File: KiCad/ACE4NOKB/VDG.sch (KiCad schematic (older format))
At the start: 32 parts, among them Q1 2N3904, Q100 2N3904, X1 CRYSTALHC49U-V 6.5MHz

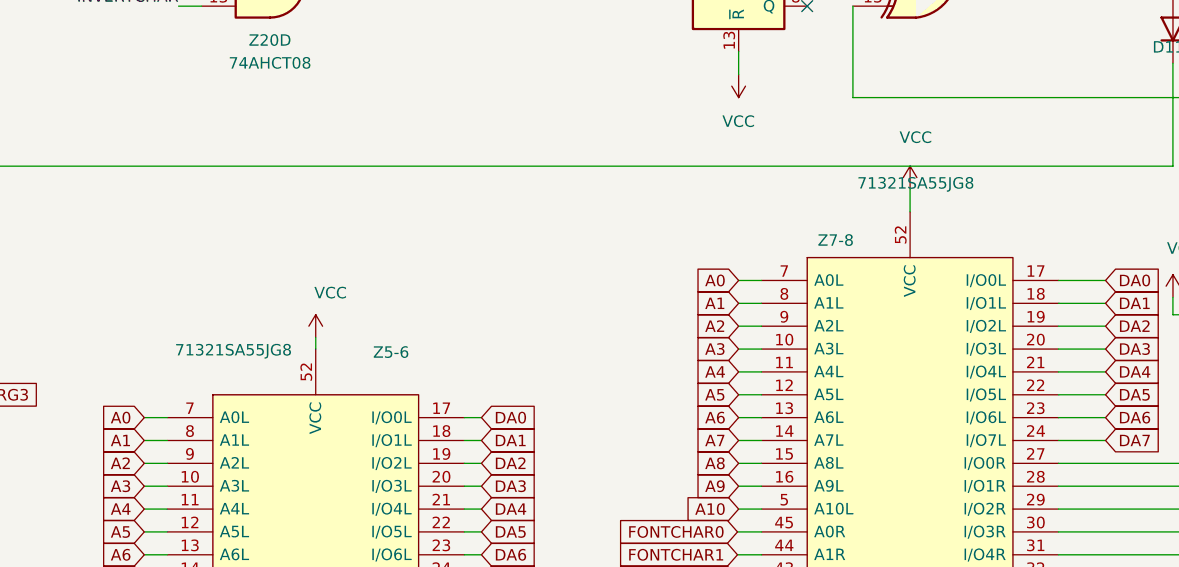
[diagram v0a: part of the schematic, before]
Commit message: Remove SMD.
Standardise Z180 and add Z380.


Signed-off-by: John Bradley <flypie@rocketmail.com>
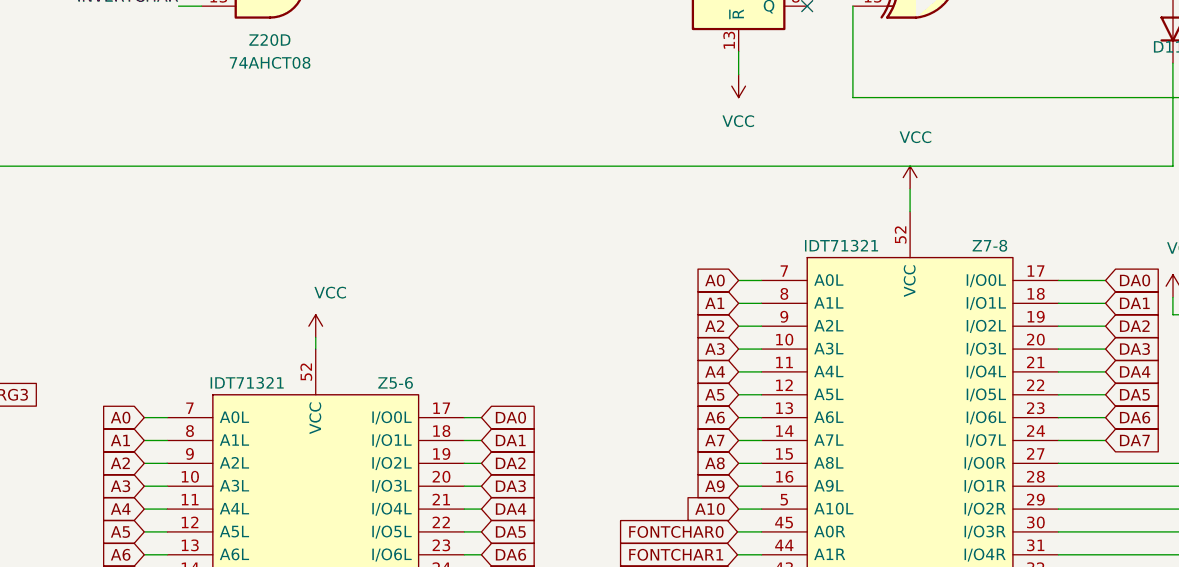
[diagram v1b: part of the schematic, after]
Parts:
- Z5-6, Z7-8: value 71321SA55JG8 -> IDT71321; footprint Package_LCC:PLCC-52_THT-Socket -> Package_LCC:PLCC-52; Description IC SRAM 16K PARALLEL 52PLCC -> SRAM 2K x 8 Dual-Port RAM Memory & Logic/ Master; Height 3.63 -> 3.8; Manufacturer_Name IDT, Integrated Device Technology Inc -> IDT (Integrated Device Technology); Manufacturer_Part_Number 71321SA55JG8 -> 7132LA100PDG
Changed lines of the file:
@@
 $Descr A4 11693 8268
 encoding utf-8
-Sheet 2 8
+Sheet 2 9
 Title "ACE4NOKB"
 Date "2020-04-30"
@@
 	0    1    1    0
 $EndComp
-$Comp
-L 7132la100pdg:IDT71321-421-52PIN-PLCC Z7-8
-U 1 1 5F80C938
-P 7000 3300
-AR Path="/5F80C938" Ref="Z7-8"  Part="1"
-AR Path="/5FA4DA0E/5F80C938" Ref="Z7-8"  Part="1"
-AR Path="/5E2F9A69/5F80C938" Ref="Z7-8"  Part="1"
-F 0 "Z7-8" H 7325 3475 50  0000 C CNN
-F 1 "71321SA55JG8" H 7675 3725 50  0000 C CNN
-F 2 "Package_LCC:PLCC-52_THT-Socket" H 7800 3950 50  0001 L CNN
-F 3 "https:/www.idt.com/document/dst/71321421-datasheet" H 7800 3850 50  0001 L CNN
-F 4 "IC SRAM 16K PARALLEL 52PLCC" H 7800 4050 50  0001 L CNN "Description"
-F 5 "3.63" H 8150 3250 50  0001 L CNN "Height"
-F 6 "IDT, Integrated Device Technology Inc" H 7800 4150 50  0001 L CNN "Manufacturer_Name"
-F 7 "71321SA55JG8" H 8150 2850 50  0001 L CNN "Manufacturer_Part_Number"
-	1    7000 3300
-	1    0    0    -1
-$EndComp
 Text GLabel 6900 5700 0    50   Input ~ 0
 ~CPUFONTRAM
@@
 AR Path="/5FA4DA0E/5F80C942" Ref="Z5-6"  Part="1"
 AR Path="/5E2F9A69/5F80C942" Ref="Z5-6"  Part="1"
-F 0 "Z5-6" H 5380 4185 50  0000 C CNN
-F 1 "71321SA55JG8" H 4690 4195 50  0000 C CNN
-F 2 "Package_LCC:PLCC-52_THT-Socket" H 5200 4550 50  0001 L CNN
-F 3 "https:/www.idt.com/document/dst/71321421-datasheet" H 5200 4450 50  0001 L CNN
-F 4 "IC SRAM 16K PARALLEL 52PLCC" H 5200 4650 50  0001 L CNN "Description"
-F 5 "3.63" H 5550 3850 50  0001 L CNN "Height"
-F 6 "IDT, Integrated Device Technology Inc" H 5200 4750 50  0001 L CNN "Manufacturer_Name"
-F 7 "71321SA55JG8" H 5550 3450 50  0001 L CNN "Manufacturer_Part_Number"
+F 0 "Z5-6" H 5400 4050 50  0000 C CNN
+F 1 "IDT71321" H 4750 4050 50  0000 C CNN
+F 2 "Package_LCC:PLCC-52" H 5200 4550 50  0001 L CNN
+F 3 "https://www.idt.com/document/dst/71321421-datasheet" H 5200 4450 50  0001 L CNN
+F 4 "SRAM 2K x 8 Dual-Port RAM Memory & Logic/ Master" H 5200 4650 50  0001 L CNN "Description"
+F 5 "3.8" H 5550 3850 50  0001 L CNN "Height"
+F 6 "IDT (Integrated Device Technology)" H 5200 4750 50  0001 L CNN "Manufacturer_Name"
+F 7 "7132LA100PDG" H 5550 3450 50  0001 L CNN "Manufacturer_Part_Number"
 	1    4400 3900
 	1    0    0    -1
@@
 	6400 900  11150 900
 Wire Wire Line
-	7650 3000 7650 2900
-Wire Wire Line
 	4400 6500 4300 6500
 Connection ~ 2275 3800
@@
 Wire Wire Line
 	6450 6250 6450 5400
+Wire Wire Line
+	7650 3000 7650 2900
+$Comp
+L 7132la100pdg:IDT71321-421-52PIN-PLCC Z7-8
+U 1 1 5F80C938
+P 7000 3300
+AR Path="/5F80C938" Ref="Z7-8"  Part="1"
+AR Path="/5FA4DA0E/5F80C938" Ref="Z7-8"  Part="1"
+AR Path="/5E2F9A69/5F80C938" Ref="Z7-8"  Part="1"
+F 0 "Z7-8" H 8000 3450 50  0000 C CNN
+F 1 "IDT71321" H 7350 3450 50  0000 C CNN
+F 2 "Package_LCC:PLCC-52" H 7800 3950 50  0001 L CNN
+F 3 "https://www.idt.com/document/dst/71321421-datasheet" H 7800 3850 50  0001 L CNN
+F 4 "SRAM 2K x 8 Dual-Port RAM Memory & Logic/ Master" H 7800 4050 50  0001 L CNN "Description"
+F 5 "3.8" H 8150 3250 50  0001 L CNN "Height"
+F 6 "IDT (Integrated Device Technology)" H 7800 4150 50  0001 L CNN "Manufacturer_Name"
+F 7 "7132LA100PDG" H 8150 2850 50  0001 L CNN "Manufacturer_Part_Number"
+	1    7000 3300
+	1    0    0    -1
+$EndComp
 $EndSCHEMATC

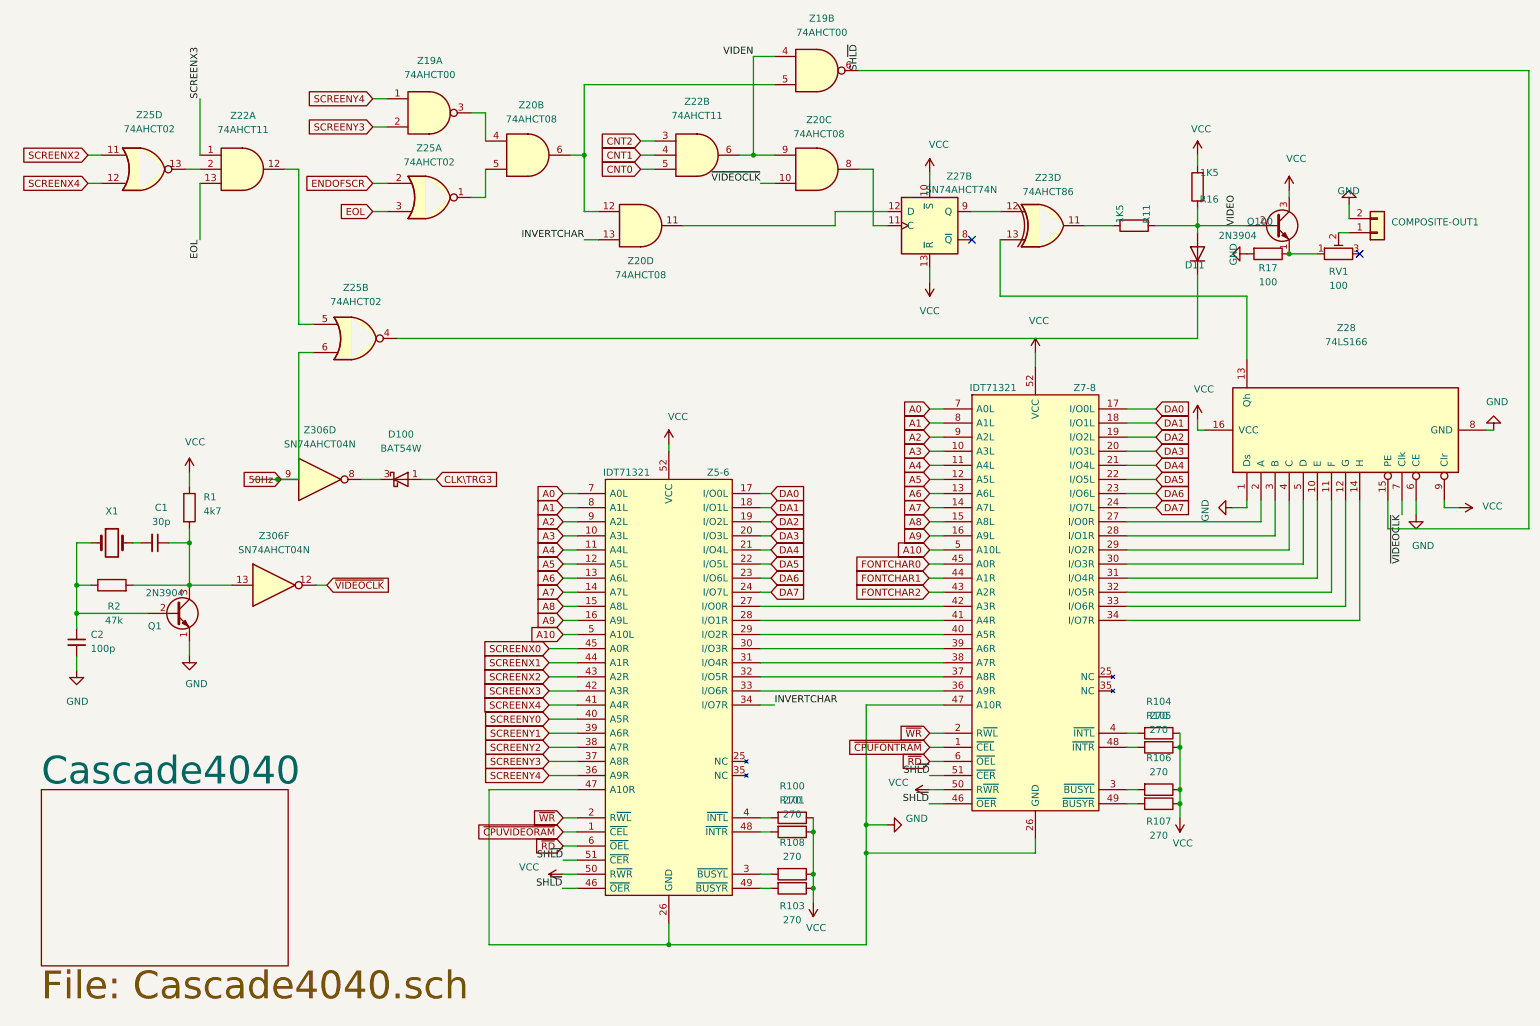
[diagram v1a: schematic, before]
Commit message: Update ACE3NOKB to reflect errors in Mem Decode. ACE5NOKB test SMT ideas. Added 180 & 380.
Signed-off-by: John Bradley <flypie@rocketmail.com>
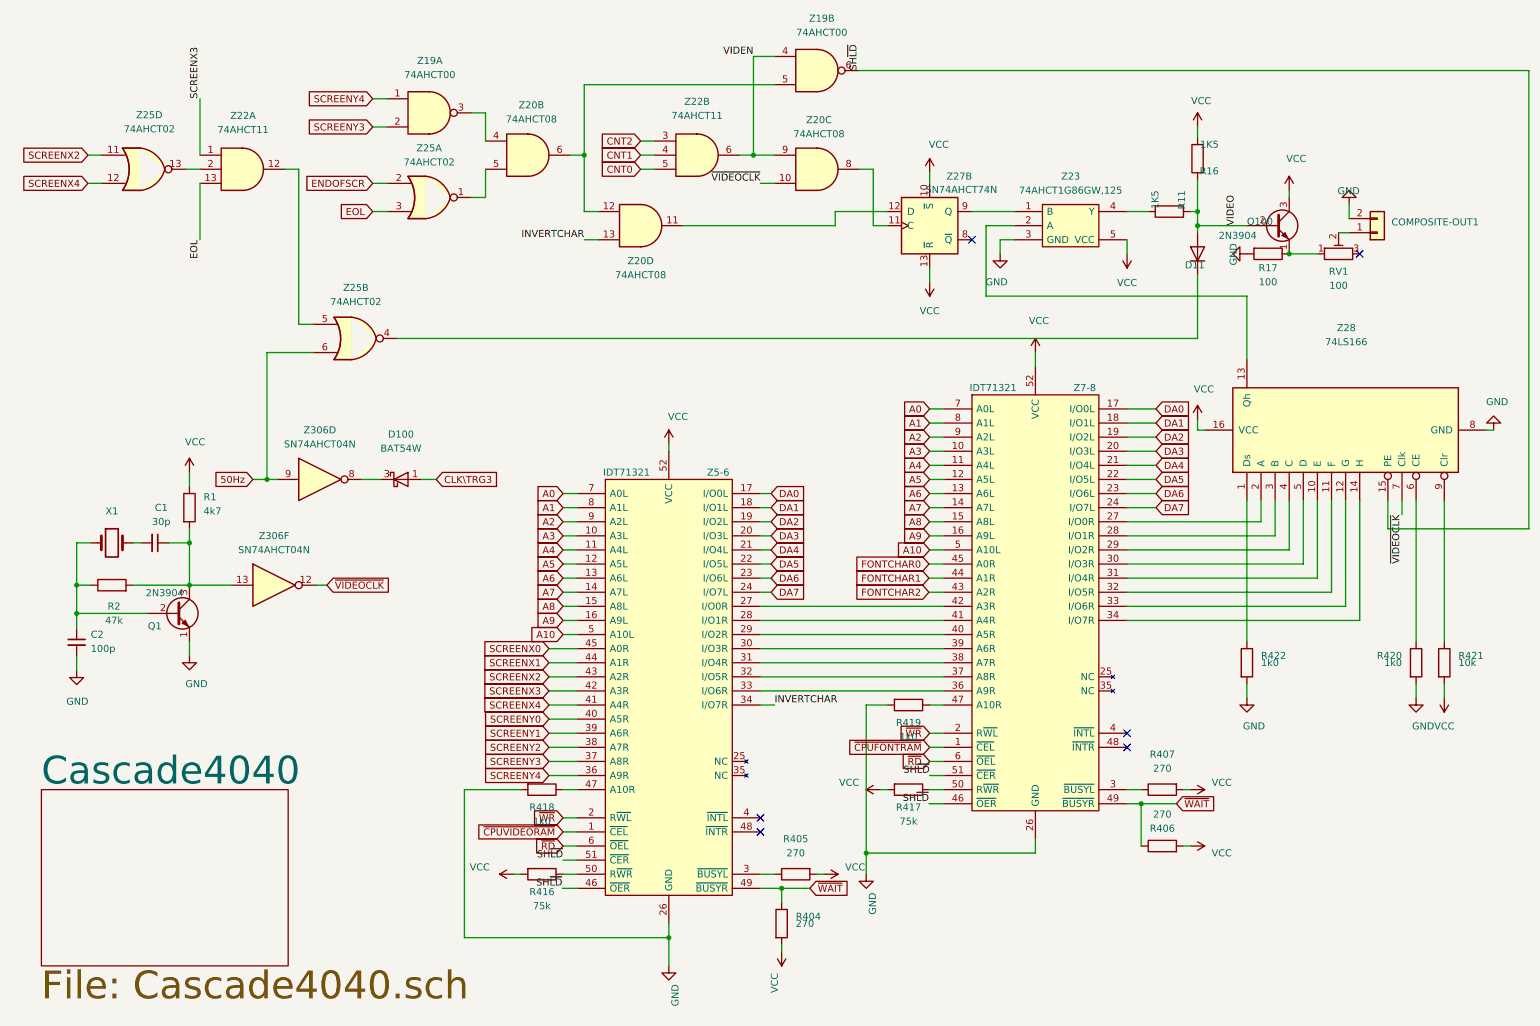
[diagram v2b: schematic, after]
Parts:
- removed R100, R101, R103, R104, R105, R106, R107, R108: 270, Resistor_THT:R_Axial_DIN0204_L3.6mm_D1.6mm_P2.54mm_Vertical, symbol Device:R
- removed Z23: 74AHCT86, Package_DIP:DIP-14_W7.62mm_Socket, symbol 74xx:74LS86
- added R404, R405, R406, R407: 270, Resistor_THT:R_Axial_DIN0204_L3.6mm_D1.6mm_P2.54mm_Vertical, symbol Device:R
- added R416, R417: 75k, Resistor_THT:R_Axial_DIN0204_L3.6mm_D1.6mm_P2.54mm_Vertical, symbol Device:R
- added R418, R419, R420, R422: 1k0, Resistor_THT:R_Axial_DIN0204_L3.6mm_D1.6mm_P2.54mm_Vertical, symbol Device:R
- added R421: 10k, Resistor_THT:R_Axial_DIN0204_L3.6mm_D1.6mm_P2.54mm_Vertical, symbol Device:R
- added Z23: 74AHCT1G86GW,125, SOT65P212X110-5N, symbol SamacSys_Parts:74AHC1G86GW,125
- Z5-6, Z7-8: footprint Package_LCC:PLCC-52 -> Package_LCC:PLCC-52_THT-Socket
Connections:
- net GND: now also R418.2, R419.2, R420.2, R422.2, Z23.3 (GND); no longer Z28.1 (Ds), Z28.6 (CE), Z5-6.47 (A10R), Z7-8.47 (A10R)
- net VCC: now also R404.2, R405.2, R406.2, R407.2, R416.2, R417.2, R421.2, Z23.5 (VCC); no longer Z28.9 (Clr), Z5-6.50 (R~WR), Z7-8.50 (R~WR)
- net at R11.2: now also Z23.4 (Y)
- net at Z27.9 (Q): now also Z23.1 (B)
- net at Z28.13 (Qh): now also Z23.2 (A)
- net at Z5-6.3 (~BUSYL): now also R405.1
- net ~WAIT: now reaches Z5-6.49 (~BUSYR)
- net ~WAIT: now also Z7-8.49 (~BUSYR), R404.1, R406.1
- net at Z7-8.3 (~BUSYL): now also R407.1
- new net: R422.1, Z28.1 (Ds)
- new net: R420.1, Z28.6 (CE)
- new net: R421.1, Z28.9 (Clr)
- new net: R419.1, Z7-8.47 (A10R)
- new net: R417.1, Z7-8.50 (R~WR)
- new net: R418.1, Z5-6.47 (A10R)
- new net: R416.1, Z5-6.50 (R~WR)
- no-connect marks 2 -> 6
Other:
- moved on the sheet: R11, R16

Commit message: Fix several problems with Chip Select. Reconnect the Data bus for the VDG to the CPU bus which has become disconnected.
Signed-off-by: John Bradley <flypie@rocketmail.com>
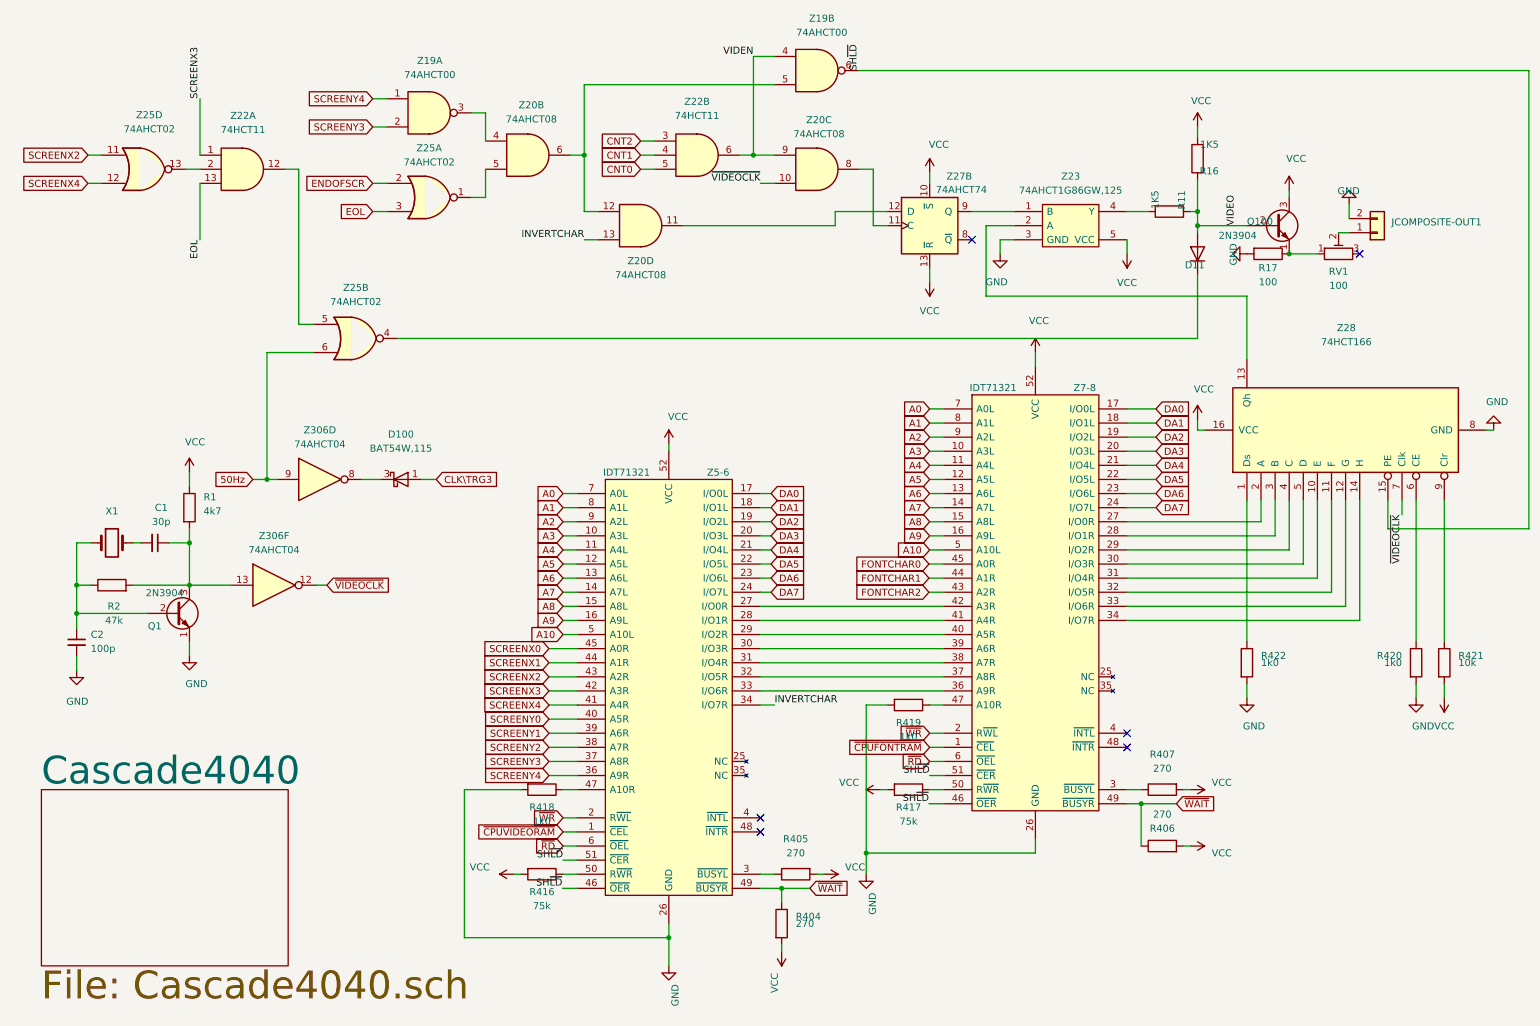
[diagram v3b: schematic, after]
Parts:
- C1: footprint Capacitor_THT:C_Disc_D3.0mm_W1.6mm_P2.50mm -> Capacitor_THT:C_Disc_D3.8mm_W2.6mm_P2.50mm; Manufacturer_Name (none) -> AVX; Manufacturer_Part_Number (none) -> SR151A300JAR
- C2: footprint Capacitor_THT:C_Disc_D3.0mm_W1.6mm_P2.50mm -> Capacitor_THT:C_Disc_D5.0mm_W2.5mm_P5.00mm; Manufacturer_Name (none) -> Vishay / BC Components; Manufacturer_Part_Number (none) -> K101J15C0GH5UH5
- D100: value BAT54W -> BAT54W,115; Manufacturer_Name (none) -> Nexperia; Manufacturer_Part_Number (none) -> BAT54W,115
- D11: Manufacturer_Name (none) -> Vishay Semiconductors; Manufacturer_Part_Number (none) -> 1N4148TR
- JCOMPOSITE-OUT1: renamed from COMPOSITE-OUT1; Manufacturer_Name (none) -> Amphenol FCI; Manufacturer_Part_Number (none) -> G800W306018EU
- Q1, Q100: Manufacturer_Name (none) -> Rectron; Manufacturer_Part_Number (none) -> 2N3904
- R1: Manufacturer_Name (none) -> Vishay; Manufacturer_Part_Number (none) -> MBA02040C4701FC100
- R11, R16: footprint Resistor_THT:R_Axial_DIN0204_L3.6mm_D1.6mm_P2.54mm_Vertical -> Resistor_THT:R_Axial_DIN0204_L3.6mm_D1.6mm_P1.90mm_Vertical; Manufacturer_Name (none) -> Vishay; Manufacturer_Part_Number (none) -> CCF071K50GKE36
- R17: footprint Resistor_THT:R_Axial_DIN0204_L3.6mm_D1.6mm_P2.54mm_Vertical -> Resistor_THT:R_Axial_DIN0204_L3.6mm_D1.6mm_P1.90mm_Vertical; Manufacturer_Name (none) -> Vishay; Manufacturer_Part_Number (none) -> PR01000101000JA500
- R2: footprint Resistor_THT:R_Axial_DIN0204_L3.6mm_D1.6mm_P2.54mm_Vertical -> Resistor_THT:R_Axial_DIN0204_L3.6mm_D1.6mm_P1.90mm_Vertical; Manufacturer_Name (none) -> Vishay; Manufacturer_Part_Number (none) -> CCF0747K0GKE36
- R404, R405, R406, R407: footprint Resistor_THT:R_Axial_DIN0204_L3.6mm_D1.6mm_P2.54mm_Vertical -> Resistor_THT:R_Axial_DIN0204_L3.6mm_D1.6mm_P1.90mm_Vertical; Manufacturer_Name (none) -> Vishay; Manufacturer_Part_Number (none) -> CCF07270RGKE36
- R416, R417: footprint Resistor_THT:R_Axial_DIN0204_L3.6mm_D1.6mm_P2.54mm_Vertical -> Resistor_THT:R_Axial_DIN0204_L3.6mm_D1.6mm_P1.90mm_Vertical; Manufacturer_Name (none) -> Vishay; Manufacturer_Part_Number (none) -> CCF0775K0GKE36
- R418, R419, R420, R422: footprint Resistor_THT:R_Axial_DIN0204_L3.6mm_D1.6mm_P2.54mm_Vertical -> Resistor_THT:R_Axial_DIN0204_L3.6mm_D1.6mm_P1.90mm_Vertical; Manufacturer_Name (none) -> Vishay; Manufacturer_Part_Number (none) -> MBB02070C1001FC100
- R421: footprint Resistor_THT:R_Axial_DIN0204_L3.6mm_D1.6mm_P2.54mm_Vertical -> Resistor_THT:R_Axial_DIN0204_L3.6mm_D1.6mm_P1.90mm_Vertical; Manufacturer_Name (none) -> Vishay; Manufacturer_Part_Number (none) -> MBA02040C1002FRP00
- RV1: footprint Potentiometer_THT:3362H1103LF -> SamacSys_Parts:3306W1101; Manufacturer_Name (none) -> Bourns; Manufacturer_Part_Number (none) -> 3306W-1-101
- X1: Manufacturer_Name (none) -> ECS; Manufacturer_Part_Number (none) -> ECS-65-20-4X
- Z19: Manufacturer_Name (none) -> Texas Instruments; Manufacturer_Part_Number (none) -> SN74AHCT00NE4
- Z20: Manufacturer_Name (none) -> Texas Instruments; Manufacturer_Part_Number (none) -> SN74AHCT08N
- Z22: value 74AHCT11 -> 74HCT11; Manufacturer_Name (none) -> Texas Instruments; Manufacturer_Part_Number (none) -> CD74HCT11M
- Z23: footprint SOT65P212X110-5N -> Strange:TSSOP5
- Z25: Manufacturer_Name (none) -> Texas Instruments; Manufacturer_Part_Number (none) -> SN74AHCT02N
- Z27: value SN74AHCT74N -> 74AHCT74; Manufacturer_Name (none) -> Texas Instruments; Manufacturer_Part_Number (none) -> SN74AHCT74N
- Z28: value 74LS166 -> 74HCT166; Manufacturer_Name (none) -> Texas Instruments; Manufacturer_Part_Number (none) -> CD74HCT166E
- Z306: value SN74AHCT04N -> 74AHCT04; Manufacturer_Name (none) -> Texas Instruments; Manufacturer_Part_Number (none) -> SN74AHCT04N
- Z5-6, Z7-8: Manufacturer_Name IDT (Integrated Device Technology) -> Renesas / IDT; Manufacturer_Part_Number 7132LA100PDG -> 71321SA55JG8
